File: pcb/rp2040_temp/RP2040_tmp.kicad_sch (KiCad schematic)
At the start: 35 parts, among them J0 USB_C_Receptacle_USB2.0, J1 BREAKOUT, J2 Conn_01x04_Female, J4 Conn_01x01_Male, J5 Conn_01x02_Female, U1 XC6206PxxxMR, U2 W25Q128JVS, U3 RP2040, U44 SRV05-4, Y0 12MHZ Crystal

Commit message: added mousebites and jst breakout
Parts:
- added J3: Conn_01x04_Male, kbd:Aio3_jst, symbol Connector:Conn_01x04_Male
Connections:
- net +5V: now also J3.1 (Pin_1)
- net GND: now also J3.4 (Pin_4)
- net USB_D+: now also J3.2 (Pin_2)
- net USB_D-: now also J3.3 (Pin_3)
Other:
- note added: "Breakout for Unified Daughterboard"
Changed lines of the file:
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@@
-(kicad_sch (version 20221206) (generator eeschema)
+(kicad_sch (version 20230121) (generator eeschema)
   (paper "A3")
   (title_block
@@
     (stroke (width 0) (type default))
   )
+  (polyline (pts (xy 66.675 105.41) (xy 66.675 128.905))
+    (stroke (width 0) (type default))
+  )
   (wire (pts (xy 74.93 185.42) (xy 74.9431 185.42))
     (stroke (width 0) (type default))
@@
     (stroke (width 0) (type default))
   )
+  (polyline (pts (xy 66.675 128.905) (xy 107.315 128.905))
+    (stroke (width 0) (type default))
+  )
   (wire (pts (xy 161.29 232.918) (xy 147.32 232.918))
     (stroke (width 0) (type default))
@@
     (stroke (width 0) (type default))
   )
+  (polyline (pts (xy 66.675 105.41) (xy 107.315 105.41))
+    (stroke (width 0) (type default))
+  )
   (wire (pts (xy 241.3 142.748) (xy 241.3 141.478))
     (stroke (width 0) (type default))
@@
   )
   (wire (pts (xy 224.79 192.278) (xy 240.03 192.278))
+    (stroke (width 0) (type default))
+  )
+  (polyline (pts (xy 107.315 128.905) (xy 107.315 105.41))
     (stroke (width 0) (type default))
   )
@@
     (effects (font (size 2.54 2.54)) (justify left bottom))
   )
+  (text "Breakout for \nUnified Daughterboard" (at 67.31 110.49 0)
+    (effects (font (size 1.27 1.27)) (justify left bottom))
+  )
   (label "RUN" (at 50.292 196.342 0) (fields_autoplaced)
     (effects (font (size 1.27 1.27)) (justify left bottom))
@@
     (effects (font (size 1.27 1.27)) (justify left bottom))
   )
+  (label "USB_D+" (at 81.28 120.65 0) (fields_autoplaced)
+    (effects (font (size 1.27 1.27)) (justify left bottom))
+  )
   (label "XOUT" (at 147.32 232.918 0) (fields_autoplaced)
     (effects (font (size 1.27 1.27)) (justify left bottom))
@@
   (label "GPIO26_ADC0" (at 240.03 260.858 180) (fields_autoplaced)
     (effects (font (size 1.27 1.27)) (justify right bottom))
+  )
+  (label "USB_D-" (at 81.28 123.19 0) (fields_autoplaced)
+    (effects (font (size 1.27 1.27)) (justify left bottom))
   )
   (label "USB_D-" (at 100.076 146.558 0) (fields_autoplaced)
@@
     (property "Intersheetrefs" "${INTERSHEET_REFS}" (at 19.98 203.9906 0)
       (effects (font (size 1.27 1.27)) (justify right) hide)
+    )
+  )
+  (global_label "+5V" (shape input) (at 81.28 118.11 0) (fields_autoplaced)
+    (effects (font (size 1.27 1.27)) (justify left))
+    (property "Intersheetrefs" "${INTERSHEET_REFS}" (at 87.5636 118.0306 0)
+      (effects (font (size 1.27 1.27)) (justify left) hide)
     )
   )
@@
     )
   )
+  (symbol (lib_id "Connector:Conn_01x04_Male") (at 76.2 120.65 0) (unit 1)
+    (in_bom yes) (on_board yes) (dnp no) (fields_autoplaced)
+    (property "Reference" "J3" (at 76.835 113.03 0)
+      (effects (font (size 1.27 1.27)))
+    )
+    (property "Value" "Conn_01x04_Male" (at 76.835 115.57 0)
+      (effects (font (size 1.27 1.27)))
+    )
+    (property "Footprint" "kbd:Aio3_jst" (at 76.2 120.65 0)
+      (effects (font (size 1.27 1.27)) hide)
+    )
+    (property "Datasheet" "~" (at 76.2 120.65 0)
+      (effects (font (size 1.27 1.27)) hide)
+    )
+    (pin "1")
+    (pin "2")
+    (pin "3")
+    (pin "4")
+    (instances
+      (project "32u4"
+        (path "/e63e39d7-6ac0-4ffd-8aa3-1841a4541b55/25c8f2a3-e897-498c-8238-899363b886a2"
+          (reference "J3") (unit 1)
+        )
+      )
+    )
+  )
   (symbol (lib_id "Device:R_Small") (at 51.0032 127.9652 90) (unit 1)
     (in_bom yes) (on_board yes) (dnp no)
@@
         )
       )
+    )
+  )
+  (symbol (lib_id "power:GND") (at 81.28 125.73 0) (unit 1)
+    (in_bom yes) (on_board yes) (dnp no)
+    (property "Reference" "#PWR02" (at 81.28 132.08 0)
+      (effects (font (size 1.27 1.27)) hide)
+    )
+    (property "Value" "GND" (at 77.47 127 0)
+      (effects (font (size 1.27 1.27)))
+    )
+    (property "Footprint" "" (at 81.28 125.73 0)
+      (effects (font (size 1.27 1.27)) hide)
+    )
+    (property "Datasheet" "" (at 81.28 125.73 0)
+      (effects (font (size 1.27 1.27)) hide)
+    )
+    (pin "1")
+    (instances
+      (project "32u4"
+        (path "/e63e39d7-6ac0-4ffd-8aa3-1841a4541b55/25c8f2a3-e897-498c-8238-899363b886a2"
+          (reference "#PWR02") (unit 1)
+        )
+      )

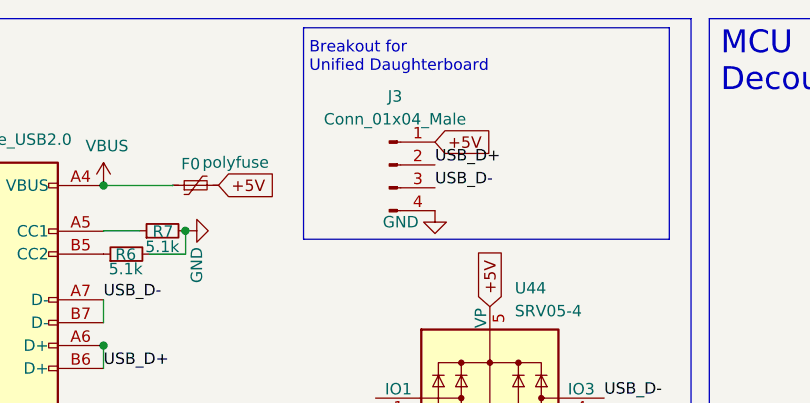
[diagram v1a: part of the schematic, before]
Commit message: added blocker cutout and daughterbaord breakout
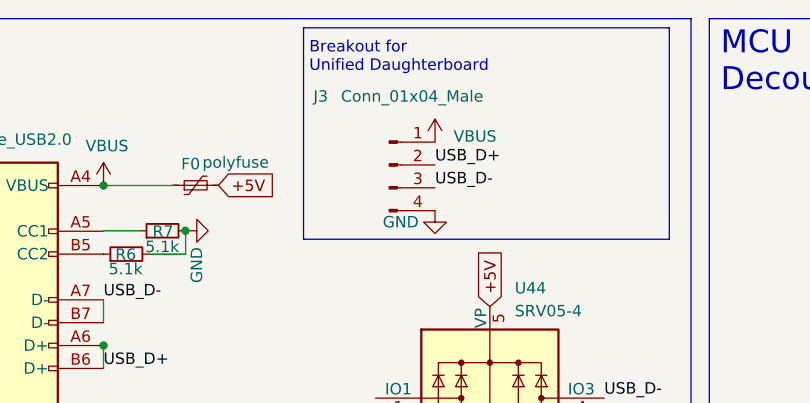
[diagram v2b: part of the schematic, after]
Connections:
- net +5V: no longer J3.1 (Pin_1)
- net VBUS: now also J3.1 (Pin_1)
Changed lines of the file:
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@@
-    )
-  )
-  (global_label "+5V" (shape input) (at 81.28 118.11 0) (fields_autoplaced)
-    (effects (font (size 1.27 1.27)) (justify left))
-    (property "Intersheetrefs" "${INTERSHEET_REFS}" (at 87.5636 118.0306 0)
-      (effects (font (size 1.27 1.27)) (justify left) hide)
     )
   )
@@
   )
   (symbol (lib_id "Connector:Conn_01x04_Male") (at 76.2 120.65 0) (unit 1)
-    (in_bom yes) (on_board yes) (dnp no) (fields_autoplaced)
-    (property "Reference" "J3" (at 76.835 113.03 0)
-      (effects (font (size 1.27 1.27)))
-    )
-    (property "Value" "Conn_01x04_Male" (at 76.835 115.57 0)
+    (in_bom yes) (on_board yes) (dnp no)
+    (property "Reference" "J3" (at 68.58 113.03 0)
+      (effects (font (size 1.27 1.27)))
+    )
+    (property "Value" "Conn_01x04_Male" (at 78.74 113.03 0)
       (effects (font (size 1.27 1.27)))
     )
@@
         )
       )
+    )
+  )
+  (symbol (lib_id "power:VBUS") (at 81.28 118.11 0) (unit 1)
+    (in_bom yes) (on_board yes) (dnp no)
+    (property "Reference" "#PWR04" (at 81.28 121.92 0)
+      (effects (font (size 1.27 1.27)) hide)
+    )
+    (property "Value" "VBUS" (at 85.725 117.475 0)
+      (effects (font (size 1.27 1.27)))
+    )
+    (property "Footprint" "" (at 81.28 118.11 0)
+      (effects (font (size 1.27 1.27)) hide)
+    )
+    (property "Datasheet" "" (at 81.28 118.11 0)
+      (effects (font (size 1.27 1.27)) hide)
+    )
+    (pin "1")
+    (instances
+      (project "32u4"
+        (path "/e63e39d7-6ac0-4ffd-8aa3-1841a4541b55/25c8f2a3-e897-498c-8238-899363b886a2"
+          (reference "#PWR04") (unit 1)
+        )
+      )

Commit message: updated routing further
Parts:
- added J6: Conn_01x04_Male, Connector_PinSocket_2.54mm:PinSocket_1x04_P2.54mm_Vertical, symbol Connector:Conn_01x04_Male
- J3: LCSC (none) -> C160404
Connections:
- net GND: now also J6.4 (Pin_4)
- net USB_D+: now also J6.2 (Pin_2)
- net USB_D-: now also J6.3 (Pin_3)
- net VBUS: now also J6.1 (Pin_1)
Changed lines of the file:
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@@
+    (effects (font (size 1.27 1.27)) (justify left bottom))
+  )
+  (label "USB_D-" (at 98.425 123.19 0) (fields_autoplaced)
     (effects (font (size 1.27 1.27)) (justify left bottom))
   )
@@
   )
   (label "QSPI_SD3" (at 147.32 204.978 0) (fields_autoplaced)
+    (effects (font (size 1.27 1.27)) (justify left bottom))
+  )
+  (label "USB_D+" (at 98.425 120.65 0) (fields_autoplaced)
     (effects (font (size 1.27 1.27)) (justify left bottom))
   )
@@
   (symbol (lib_id "Connector:Conn_01x04_Male") (at 76.2 120.65 0) (unit 1)
     (in_bom yes) (on_board yes) (dnp no)
-    (property "Reference" "J3" (at 68.58 113.03 0)
-      (effects (font (size 1.27 1.27)))
-    )
-    (property "Value" "Conn_01x04_Male" (at 78.74 113.03 0)
+    (property "Reference" "J3" (at 73.66 120.65 0)
+      (effects (font (size 1.27 1.27)))
+    )
+    (property "Value" "Conn_01x04_Male" (at 80.01 114.935 0)
       (effects (font (size 1.27 1.27)))
     )
@@
     )
     (property "Datasheet" "~" (at 76.2 120.65 0)
+      (effects (font (size 1.27 1.27)) hide)
+    )
+    (property "LCSC" " C160404" (at 76.2 120.65 0)
       (effects (font (size 1.27 1.27)) hide)
     )
@@
     )
   )
+  (symbol (lib_id "Connector:Conn_01x04_Male") (at 93.345 120.65 0) (unit 1)
+    (in_bom yes) (on_board yes) (dnp no)
+    (property "Reference" "J6" (at 91.44 120.65 0)
+      (effects (font (size 1.27 1.27)))
+    )
+    (property "Value" "Conn_01x04_Male" (at 100.965 114.3 0)
+      (effects (font (size 1.27 1.27)))
+    )
+    (property "Footprint" "Connector_PinSocket_2.54mm:PinSocket_1x04_P2.54mm_Vertical" (at 93.345 120.65 0)
+      (effects (font (size 1.27 1.27)) hide)
+    )
+    (property "Datasheet" "~" (at 93.345 120.65 0)
+      (effects (font (size 1.27 1.27)) hide)
+    )
+    (pin "1")
+    (pin "2")
+    (pin "3")
+    (pin "4")
+    (instances
+      (project "32u4"
+        (path "/e63e39d7-6ac0-4ffd-8aa3-1841a4541b55/25c8f2a3-e897-498c-8238-899363b886a2"
+          (reference "J6") (unit 1)
+        )
+      )
+    )
+  )
   (symbol (lib_id "power:GND") (at 87.376 161.798 0) (unit 1)
     (in_bom yes) (on_board yes) (dnp no)
@@
     )
   )
+  (symbol (lib_id "power:VBUS") (at 98.425 118.11 0) (unit 1)
+    (in_bom yes) (on_board yes) (dnp no)
+    (property "Reference" "#PWR010" (at 98.425 121.92 0)
+      (effects (font (size 1.27 1.27)) hide)
+    )
+    (property "Value" "VBUS" (at 102.87 117.475 0)
+      (effects (font (size 1.27 1.27)))
+    )
+    (property "Footprint" "" (at 98.425 118.11 0)
+      (effects (font (size 1.27 1.27)) hide)
+    )
+    (property "Datasheet" "" (at 98.425 118.11 0)
+      (effects (font (size 1.27 1.27)) hide)
+    )
+    (pin "1")
+    (instances
+      (project "32u4"
+        (path "/e63e39d7-6ac0-4ffd-8aa3-1841a4541b55/25c8f2a3-e897-498c-8238-899363b886a2"
+          (reference "#PWR010") (unit 1)
+        )
+      )
+    )
+  )
   (symbol (lib_id "Device:R") (at 32.004 228.346 90) (unit 1)
     (in_bom yes) (on_board yes) (dnp no) (fields_autoplaced)
@@
         )
       )
+    )
+  )
+  (symbol (lib_id "power:GND") (at 98.425 125.73 0) (unit 1)
+    (in_bom yes) (on_board yes) (dnp no)
+    (property "Reference" "#PWR015" (at 98.425 132.08 0)
+      (effects (font (size 1.27 1.27)) hide)
+    )
+    (property "Value" "GND" (at 94.615 127 0)
+      (effects (font (size 1.27 1.27)))
+    )
+    (property "Footprint" "" (at 98.425 125.73 0)
+      (effects (font (size 1.27 1.27)) hide)
+    )
+    (property "Datasheet" "" (at 98.425 125.73 0)
+      (effects (font (size 1.27 1.27)) hide)
+    )
+    (pin "1")
+    (instances
+      (project "32u4"
+        (path "/e63e39d7-6ac0-4ffd-8aa3-1841a4541b55/25c8f2a3-e897-498c-8238-899363b886a2"
+          (reference "#PWR015") (unit 1)
+        )
+      )
